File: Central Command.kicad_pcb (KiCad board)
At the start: 4 copper layers, 16 parts, among them P1 CONN_01X06, P2 CONN_01X02, U1 STM32F030C8, U2 MCP1700T-3302E/TT_

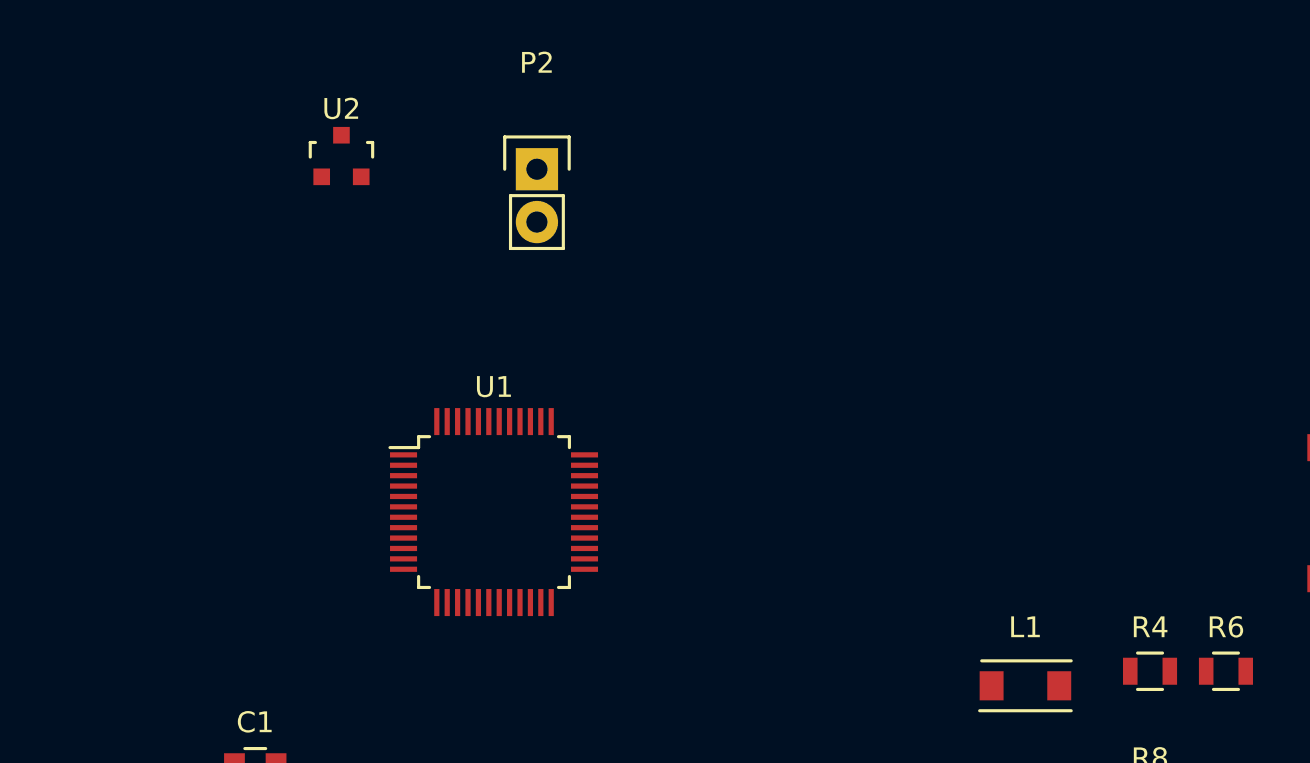
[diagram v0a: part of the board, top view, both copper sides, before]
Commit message: Added Crystal to the schematic and layout
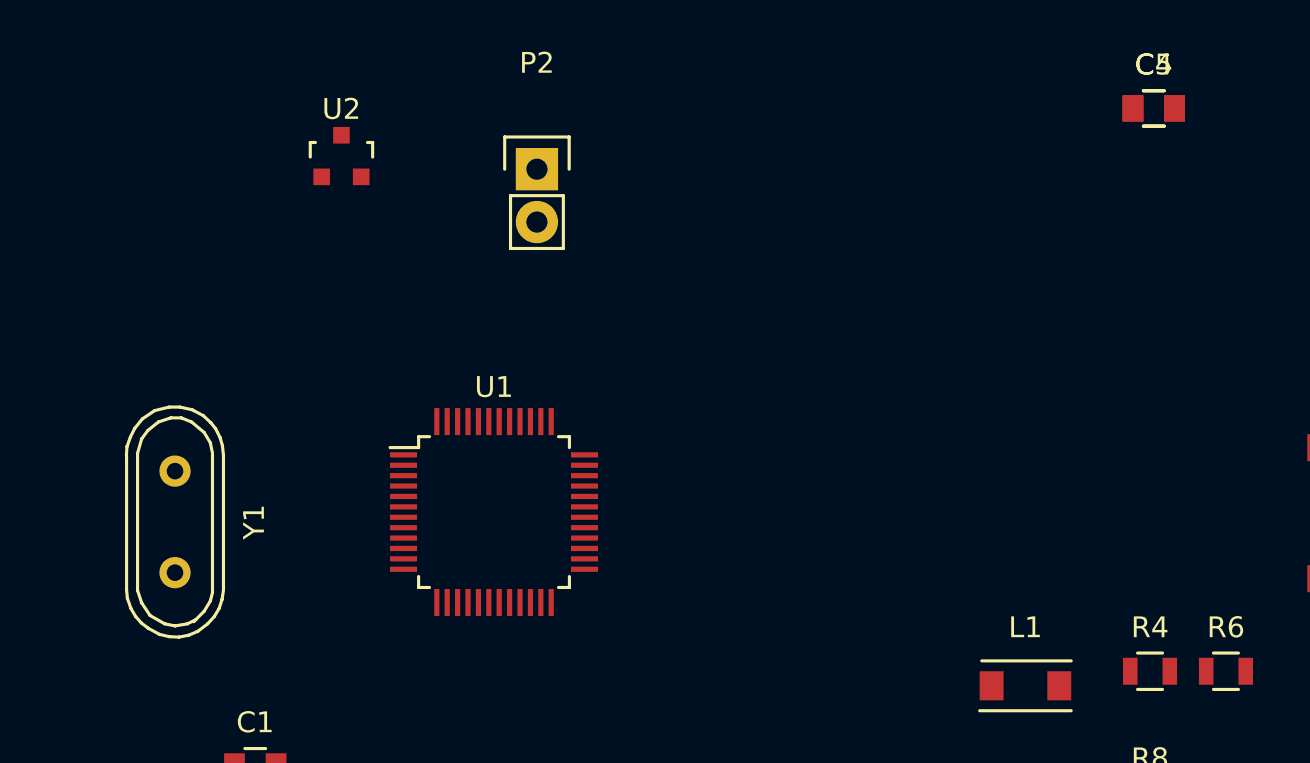
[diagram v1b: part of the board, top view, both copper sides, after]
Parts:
- added C4, C5: 20P, Capacitors_SMD:C_0805, F.Cu at (160.8, 88.3)
- added Y1: Crystal, Crystals:Crystal_HC49-U_Vertical, F.Cu at (113.7, 108.1)

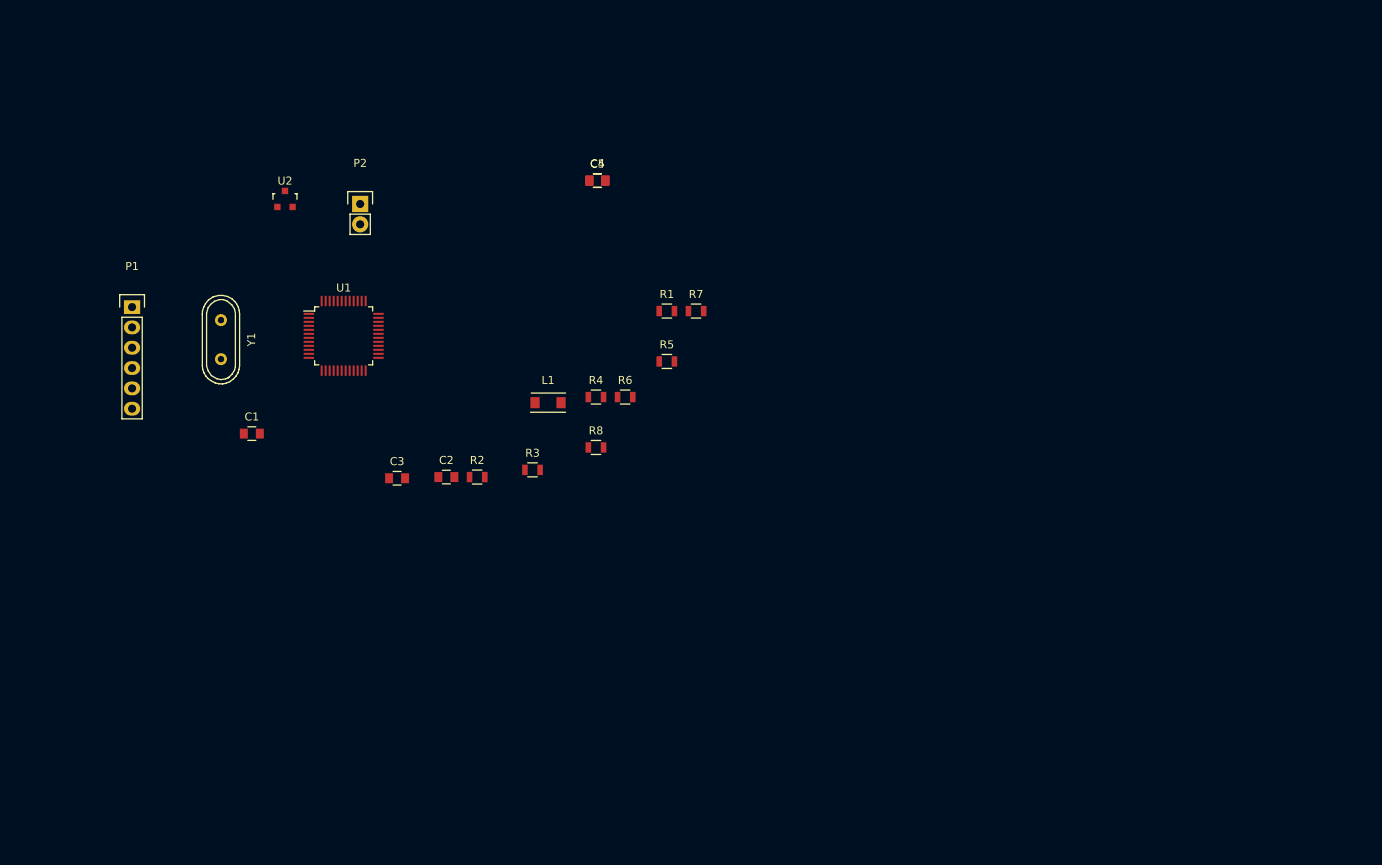
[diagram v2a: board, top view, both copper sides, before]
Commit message: Associated footprints, created footprints for 2mm connector and did prelim placement
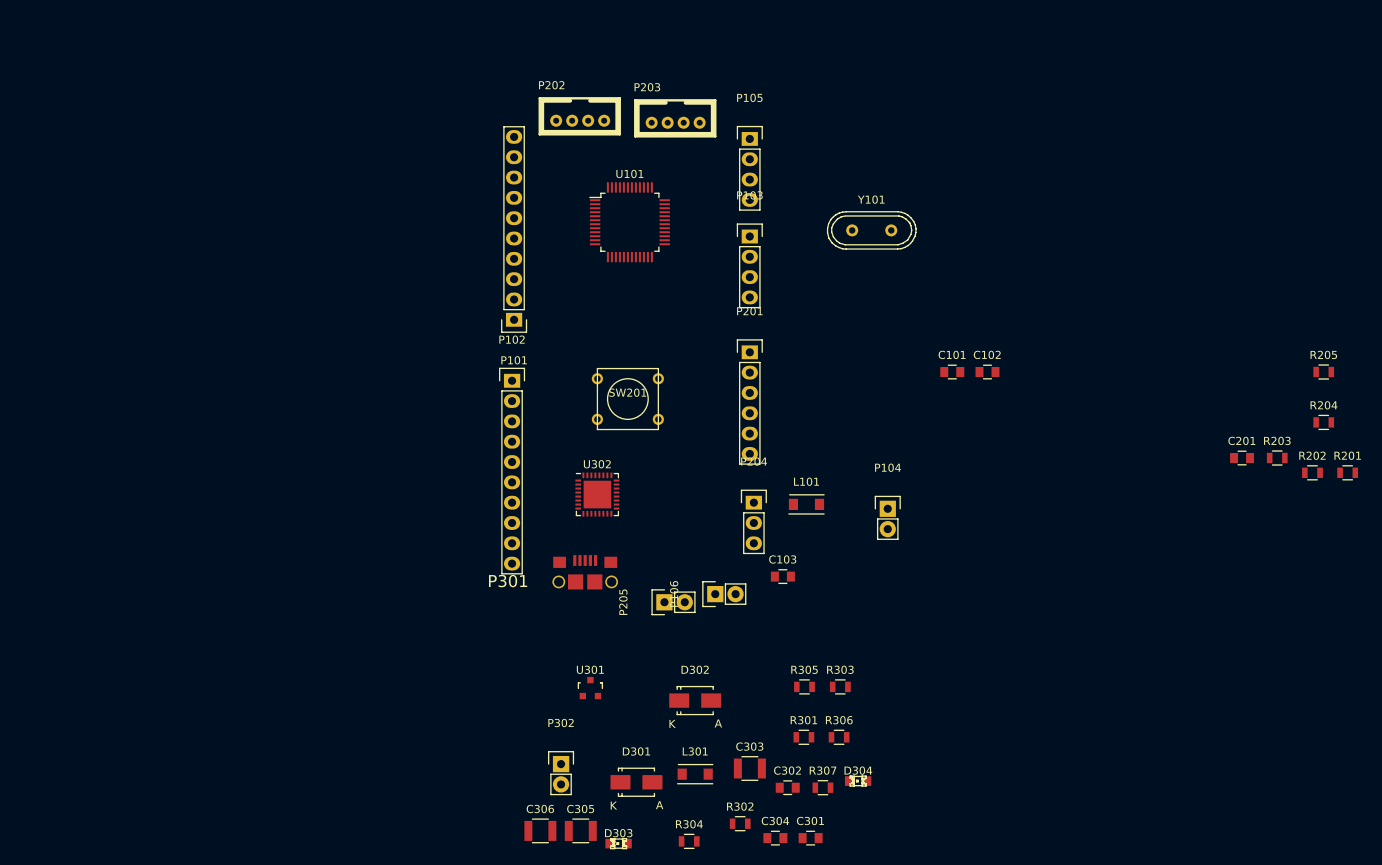
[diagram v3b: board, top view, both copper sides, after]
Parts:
- removed C1, C2, C3: C, Capacitors_SMD:C_0805
- removed C4, C5: 20P, Capacitors_SMD:C_0805
- removed L1: INDUCTOR, Inductors_NEOSID:Neosid_Inductor_SM1206
- removed P1: CONN_01X06, Pin_Headers:Pin_Header_Straight_1x06
- removed P2: CONN_01X02, Pin_Headers:Pin_Header_Straight_1x02
- removed R1, R3, R4, R5, R6, R7, R8: R, Resistors_SMD:R_0805
- removed R2: 0, Resistors_SMD:R_0805
- removed U1: STM32F030C8, Housings_QFP:LQFP-48_7x7mm_Pitch0.5mm
- removed U2: MCP1700T-3302E/TT_, Housings_SOT-23_SOT-143_TSOT-6:SOT-23
- removed Y1: Crystal, Crystals:Crystal_HC49-U_Vertical
- added C101: C, Capacitors_SMD:C_0805, F.Cu at (205.1, 112.2)
- added C102: 20P, Capacitors_SMD:C_0805, F.Cu at (209.5, 112.2)
- added C103: 20P, Capacitors_SMD:C_0805, F.Cu at (184.0, 137.8)
- added C201: C, Capacitors_SMD:C_0805, F.Cu at (241.4, 122.9)
- added C301: .1U, Capacitors_SMD:C_0805, F.Cu at (187.4, 170.5)
- added C302: .1U, Capacitors_SMD:C_0805, F.Cu at (184.6, 164.2)
- added C303: 4.7U, Capacitors_SMD:C_1210, F.Cu at (179.8, 161.8)
- added C304: .1U, Capacitors_SMD:C_0805, F.Cu at (183.0, 170.5)
- added C305: 10U, Capacitors_SMD:C_1210, F.Cu at (158.7, 169.6)
- added C306: 10U, Capacitors_SMD:C_1210, F.Cu at (153.7, 169.6)
- added D301: D_Schottky, Diodes_SMD:Diode-SMA_Standard, F.Cu at (165.7, 163.5)
- added D302: D_Schottky, Diodes_SMD:Diode-SMA_Standard, F.Cu at (173.0, 153.3)
- added D303: LED, LEDs:LED-0805, F.Cu at (163.4, 171.1)
- added D304: LED, LEDs:LED-0805, F.Cu at (193.4, 163.3)
- added L101: INDUCTOR, Inductors_NEOSID:Neosid_Inductor_SM1206, F.Cu at (186.9, 128.7)
- added L301: FERRITE, Inductors_NEOSID:Neosid_Inductor_SM1206, F.Cu at (173.0, 162.5)
- added P101: CONN_01X10, Pin_Headers:Pin_Header_Straight_1x10, F.Cu at (150.4, 105.7)
- added P102: CONN_01X10, Pin_Headers:Pin_Header_Straight_1x10, F.Cu at (150.1, 113.3)
- added P103: CONN_01X04, Pin_Headers:Pin_Header_Straight_1x04, F.Cu at (179.8, 95.2)
- added P104: CONN_01X02, Pin_Headers:Pin_Header_Straight_1x02, F.Cu at (197.1, 129.3)
- added P105: CONN_01X04, Pin_Headers:Pin_Header_Straight_1x04, F.Cu at (179.8, 83.1)
- added P106: CONN_01X02, Pin_Headers:Pin_Header_Straight_1x02, F.Cu at (175.5, 140.0)
- added P201: CONN_01X06, Pin_Headers:Pin_Header_Straight_1x06, F.Cu at (179.8, 109.7)
- added P202: CONN_01X04, CentralCommand:Grove-2mm, F.Cu at (163.6, 78.0)
- added P203: CONN_01X04, CentralCommand:Grove-2mm, F.Cu at (175.5, 78.2)
- added P204: CONN_01X03, Pin_Headers:Pin_Header_Straight_1x03, F.Cu at (180.3, 128.5)
- added P205: CONN_01X02, Pin_Headers:Pin_Header_Straight_1x02, F.Cu at (169.2, 141.0)
- added P301: USB_B, CentralCommand:10118193, F.Cu at (159.3, 138.4)
- added P302: CONN_01X02, Pin_Headers:Pin_Header_Straight_1x02, F.Cu at (156.2, 161.2)
- added R201: R, Resistors_SMD:R_0805, F.Cu at (254.6, 124.8)
- added R202: R, Resistors_SMD:R_0805, F.Cu at (250.2, 124.8)
- added R203: 0, Resistors_SMD:R_0805, F.Cu at (245.8, 122.9)
- added R204: R, Resistors_SMD:R_0805, F.Cu at (251.6, 118.5)
- added R205: R, Resistors_SMD:R_0805, F.Cu at (251.6, 112.2)
- added R301: 0, Resistors_SMD:R_0805, F.Cu at (186.6, 157.9)
- added R302: 0, Resistors_SMD:R_0805, F.Cu at (178.6, 168.7)
- added R303: 0, Resistors_SMD:R_0805, F.Cu at (191.1, 151.6)
- added R304: NOPE, Resistors_SMD:R_0805, F.Cu at (172.3, 170.9)
- added R305: NOPE, Resistors_SMD:R_0805, F.Cu at (186.7, 151.6)
- added R306: 270, Resistors_SMD:R_0805, F.Cu at (191.0, 157.9)
- added R307: 270, Resistors_SMD:R_0805, F.Cu at (189.0, 164.2)
- added SW201: SW_PUSH, Buttons_Switches_ThroughHole:SW_PUSH_SMALL, F.Cu at (164.6, 115.6)
- added U101: STM32F030C8, Housings_QFP:LQFP-48_7x7mm_Pitch0.5mm, F.Cu at (164.8, 93.5)
- added U301: MCP1700T-3302E/TT_, Housings_SOT-23_SOT-143_TSOT-6:SOT-23, F.Cu at (159.9, 151.7)
- added U302: FT232RQ, Housings_DFN_QFN:QFN-32-1EP_5x5mm_Pitch0.5mm, F.Cu at (160.8, 127.5)
- added Y101: Crystal, Crystals:Crystal_HC49-U_Vertical, F.Cu at (195.1, 94.5)

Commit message: Changed board outline (now 2x2) and placed headers around the outside based on pin connections.
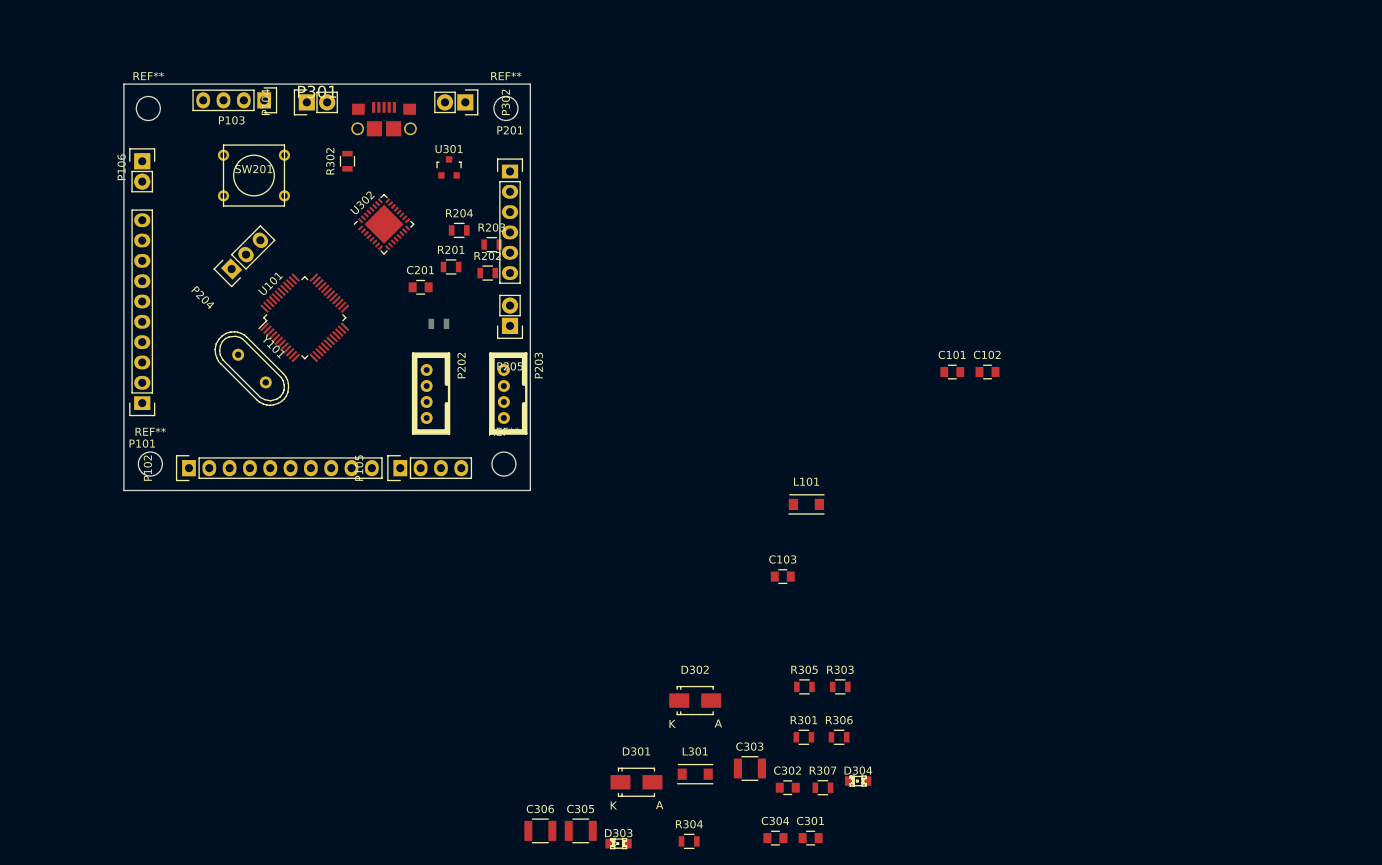
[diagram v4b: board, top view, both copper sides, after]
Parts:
- added REF**: MountingHole_3mm, Mounting_Holes:MountingHole_3mm, F.Cu at (104.6, 79.2)
- added REF**: MountingHole_3mm, Mounting_Holes:MountingHole_3mm, F.Cu at (104.9, 123.7)
- added REF**: MountingHole_3mm, Mounting_Holes:MountingHole_3mm, F.Cu at (149.1, 123.7)
- added REF**: MountingHole_3mm, Mounting_Holes:MountingHole_3mm, F.Cu at (149.4, 79.2)
- P101: value CONN_01X10 -> GPIO 1
- P102: value CONN_01X10 -> GPIO 2
- P103: value CONN_01X04 -> SPI
- P104: value CONN_01X02 -> SENSOR I2C
- P105: value CONN_01X04 -> ADC
- P106: value CONN_01X02 -> SERIAL
- P201: value CONN_01X06 -> PROGRAMMING
- P204: value CONN_01X03 -> BOOT0
- P205: value CONN_01X02 -> MCO
- P302: value CONN_01X02 -> ALT PWR
- R205: moved to B.Cu
- U301: value MCP1700T-3302E/TT_ -> MCP1700T
- moved R201 115.0 mm to (142.5, 99.1)
- moved R205 110.8 mm to (141.0, 106.2)
- moved R204 110.7 mm to (143.5, 94.5)
- moved R202 106.1 mm to (147.1, 99.8)
- moved C201 104.9 mm to (138.7, 101.6)
- moved R203 101.7 mm to (147.6, 96.3)
- moved R302 96.3 mm to (129.5, 85.9), turned to 90 degrees
- moved P106 89.8 mm to (103.9, 85.9), turned to 0 degrees
- moved P104 88.6 mm to (124.5, 78.5), turned to 90 degrees
- moved P302 83.6 mm to (144.3, 78.5), turned to 270 degrees
- moved Y101 79.4 mm to (117.6, 111.8), turned to 315 degrees
- moved P204 71.5 mm to (115.1, 99.3), turned to 135 degrees
- moved U301 67.4 mm to (142.2, 86.6)
- moved P103 63.0 mm to (119.1, 78.2), turned to 270 degrees
- moved P301 62.0 mm to (134.1, 81.8)
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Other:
- board outline added: 50.8 x 50.8 mm

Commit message: Added ground and power layers.
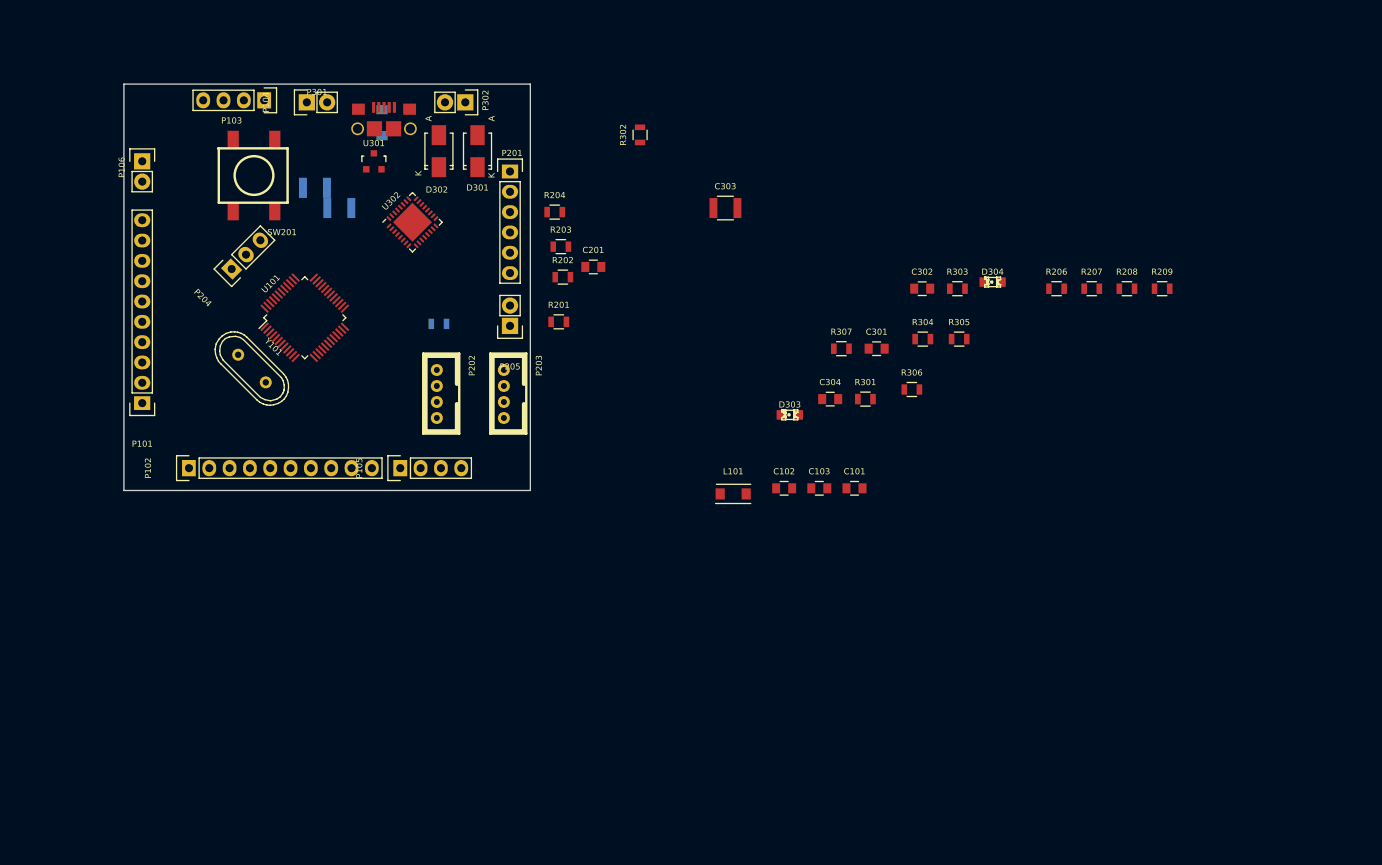
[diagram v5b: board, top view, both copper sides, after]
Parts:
- removed REF** (x4): MountingHole_3mm, Mounting_Holes:MountingHole_3mm
- added R206: 0, Resistors_SMD:R_0805, F.Cu at (218.2, 101.8)
- added R207: 0, Resistors_SMD:R_0805, F.Cu at (222.6, 101.8)
- added R208: 0, Resistors_SMD:R_0805, F.Cu at (227.0, 101.8)
- added R209: 0, Resistors_SMD:R_0805, F.Cu at (231.4, 101.8)
- C305, C306, L301: moved to B.Cu
- P101: value GPIO 1 -> CONN_01X10
- P102: value GPIO 2 -> CONN_01X10
- P103: value SPI -> CONN_01X04
- P104: value SENSOR I2C -> CONN_01X02
- P105: value ADC -> CONN_01X04
- P106: value SERIAL -> CONN_01X02
- P201: value PROGRAMMING -> CONN_01X06
- P204: value BOOT0 -> CONN_01X03
- P205: value MCO -> CONN_01X02
- P302: value ALT PWR -> CONN_01X02
- SW201: value SW_PUSH -> FSM2JSMAA-ND; footprint Buttons_Switches_ThroughHole:SW_PUSH_SMALL -> CentralCommand:FSM2JSMAA-ND
- U301: value MCP1700T -> MCP1700T-3302E/TT_
- moved L301 90.4 mm to (133.9, 81.0), turned to 270 degrees
- moved C306 85.2 mm to (125.5, 89.2)
- moved C305 83.5 mm to (128.5, 91.7)
- moved D301 81.4 mm to (145.8, 84.6), turned to 90 degrees
- moved D302 75.8 mm to (141.0, 84.6), turned to 90 degrees
- moved C303 70.1 mm to (176.8, 91.7)
- moved R304 69.2 mm to (201.5, 108.1)
- moved C302 64.6 mm to (201.4, 101.8)
- moved D304 64.6 mm to (210.2, 100.9)
- moved C301 61.7 mm to (195.7, 109.3)
- moved D303 57.7 mm to (184.8, 117.5)
- moved C304 55.3 mm to (189.9, 115.6)
- moved R307 54.9 mm to (191.3, 109.3)
- moved R303 51.9 mm to (205.8, 101.8)
- moved R305 47.6 mm to (206.0, 108.1)
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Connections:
- C101 pad 2: Net-(C101-Pad2) -> GND
- P203 pad 1: GND -> Net-(P203-Pad1)
- P203 pad 2: /Comm/PWR -> Net-(P203-Pad2)
- P203 pad 3: /Comm/SCL -> Net-(P203-Pad3)
- P203 pad 4: /Comm/SDA -> Net-(P203-Pad4)
- U101 pad 19: /ADC_IN8 -> /ADC_IN9
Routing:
- added copper zone on PWR, net /Comm/PWR
- added copper zone on GND, net GND
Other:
- net class Default: clearance 0.2 -> 0.1524; trace_width 0.25 -> 0.1524; via_dia 0.6 -> 0.6858; via_drill 0.4 -> 0.3302
- rule trace_clearance: 0.2 -> 0.1524
- rule trace_min: 0.2 -> 0.1524
- rule via_min_drill: 0.3 -> 0.3302
- rule via_min_size: 0.4 -> 0.6858
